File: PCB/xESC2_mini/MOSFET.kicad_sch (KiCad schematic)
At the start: 9 parts, among them J8 Conn_02x02_Counter_Clockwise, Q5 BSC026N08NS5, Q6 BSC026N08NS5

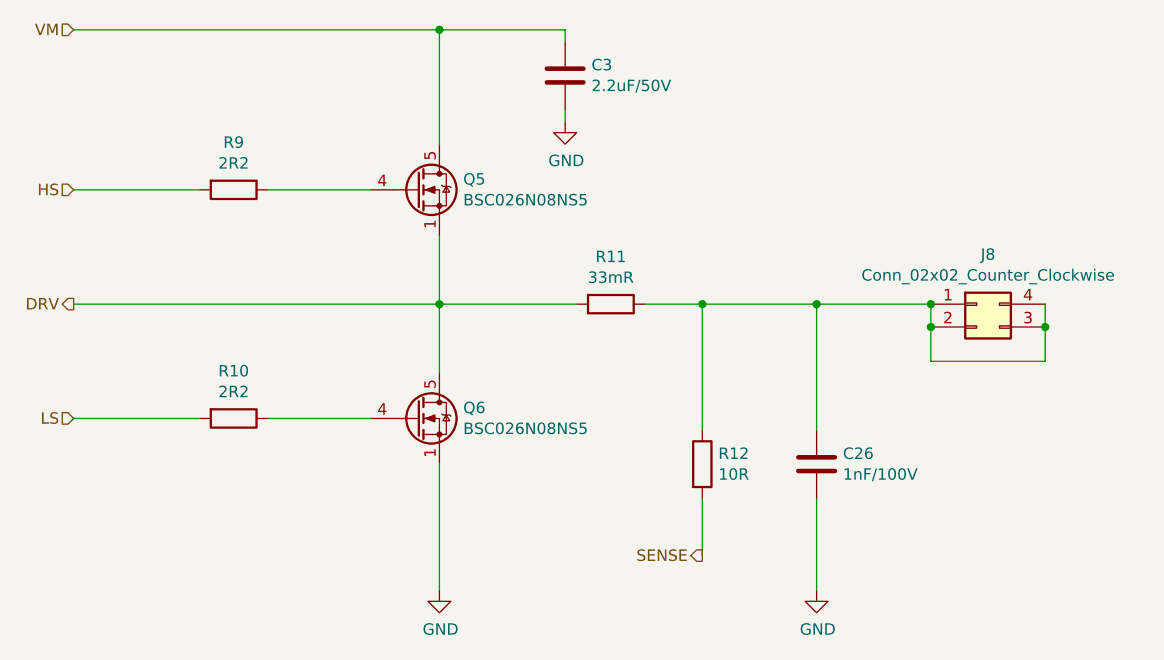
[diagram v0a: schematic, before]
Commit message: wip - most routing for RP2040 done
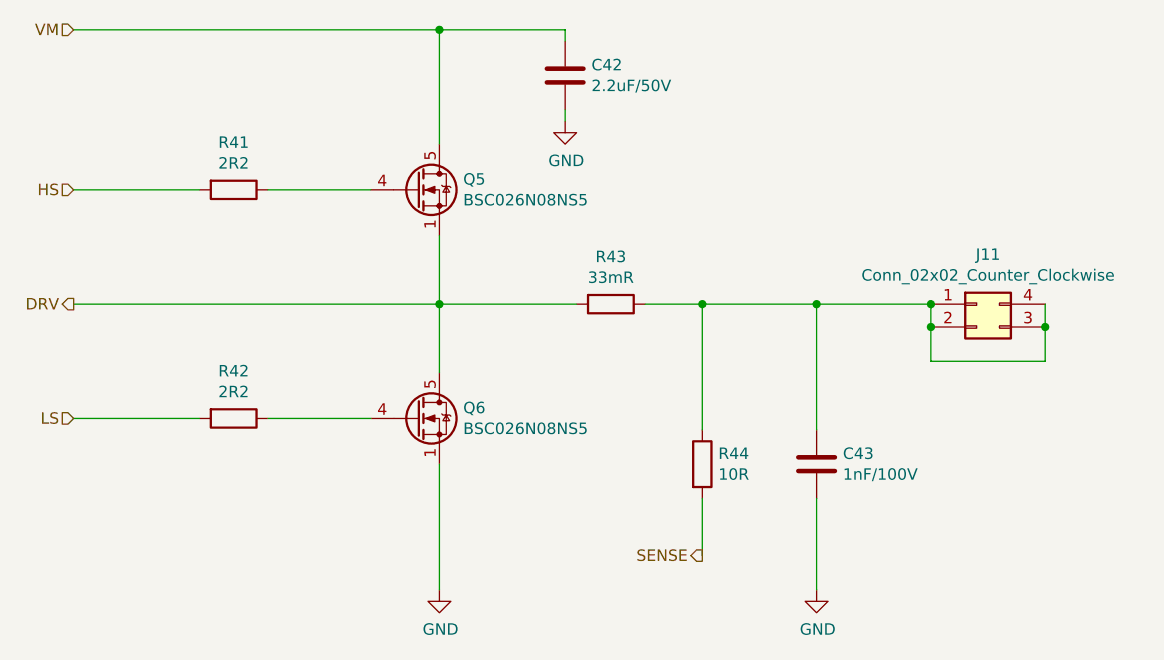
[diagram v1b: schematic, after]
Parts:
- renumbered C3 to C42, C26 to C43, J8 to J11, R9 to R41, R10 to R42, R11 to R43, R12 to R44
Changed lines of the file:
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@@
   (symbol (lib_id "Device:R") (at 195.58 83.82 270)
     (in_bom yes) (on_board yes)
-    (property "Reference" "R11" (id 0) (at 195.58 78.5622 90))
+    (property "Reference" "R43" (id 0) (at 195.58 78.5622 90))
     (property "Value" "33mR" (id 1) (at 195.58 80.8736 90))
     (property "Footprint" "Resistor_SMD:R_2512_6332Metric" (id 2) (at 195.58 82.042 90)
@@
   (symbol (lib_id "Device:R") (at 153.67 71.12 270)
     (in_bom yes) (on_board yes)
-    (property "Reference" "R9" (id 0) (at 153.67 65.8622 90))
+    (property "Reference" "R41" (id 0) (at 153.67 65.8622 90))
     (property "Value" "2R2" (id 1) (at 153.67 68.1736 90))
     (property "Footprint" "Resistor_SMD:R_0603_1608Metric" (id 2) (at 153.67 69.342 90)
@@
   (symbol (lib_id "Device:R") (at 153.67 96.52 270)
     (in_bom yes) (on_board yes)
-    (property "Reference" "R10" (id 0) (at 153.67 91.2622 90))
+    (property "Reference" "R42" (id 0) (at 153.67 91.2622 90))
     (property "Value" "2R2" (id 1) (at 153.67 93.5736 90))
     (property "Footprint" "Resistor_SMD:R_0603_1608Metric" (id 2) (at 153.67 94.742 90)
@@
   (symbol (lib_id "Device:R") (at 205.74 101.6 0)
     (in_bom yes) (on_board yes)
-    (property "Reference" "R12" (id 0) (at 207.518 100.4316 0)
+    (property "Reference" "R44" (id 0) (at 207.518 100.4316 0)
       (effects (font (size 1.27 1.27)) (justify left))
     )
@@
   (symbol (lib_id "power:GND") (at 176.53 115.57 0)
     (in_bom yes) (on_board yes)
-    (property "Reference" "#PWR0105" (id 0) (at 176.53 121.92 0)
+    (property "Reference" "#PWR042" (id 0) (at 176.53 121.92 0)
       (effects (font (size 1.27 1.27)) hide)
     )
@@
   (symbol (lib_id "Device:C") (at 190.5 58.42 0)
     (in_bom yes) (on_board yes)
-    (property "Reference" "C3" (id 0) (at 193.421 57.2516 0)
+    (property "Reference" "C42" (id 0) (at 193.421 57.2516 0)
       (effects (font (size 1.27 1.27)) (justify left))
     )
@@
   (symbol (lib_id "power:GND") (at 190.5 63.5 0)
     (in_bom yes) (on_board yes)
-    (property "Reference" "#PWR0106" (id 0) (at 190.5 69.85 0)
+    (property "Reference" "#PWR043" (id 0) (at 190.5 69.85 0)
       (effects (font (size 1.27 1.27)) hide)
     )
@@
   (symbol (lib_id "Device:C") (at 218.44 101.6 0)
     (in_bom yes) (on_board yes)
-    (property "Reference" "C26" (id 0) (at 221.361 100.4316 0)
+    (property "Reference" "C43" (id 0) (at 221.361 100.4316 0)
       (effects (font (size 1.27 1.27)) (justify left))
     )
@@
   (symbol (lib_id "power:GND") (at 218.44 115.57 0)
     (in_bom yes) (on_board yes)
-    (property "Reference" "#PWR0118" (id 0) (at 218.44 121.92 0)
+    (property "Reference" "#PWR044" (id 0) (at 218.44 121.92 0)
       (effects (font (size 1.27 1.27)) hide)
     )
@@
   (symbol (lib_id "Connector_Generic:Conn_02x02_Counter_Clockwise") (at 236.22 83.82 0)
     (in_bom yes) (on_board yes)
-    (property "Reference" "J8" (id 0) (at 237.49 78.3082 0))
+    (property "Reference" "J11" (id 0) (at 237.49 78.3082 0))
     (property "Value" "Conn_02x02_Counter_Clockwise" (id 1) (at 237.49 80.6196 0))
     (property "Footprint" "Connector_PinHeader_2.54mm:PinHeader_2x02_P2.54mm_Vertical" (id 2) (at 236.22 83.82 0)
